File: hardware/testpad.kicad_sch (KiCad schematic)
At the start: 14 parts, among them U2 ESP32-C6-WROOM-1, U3 TPS62840YBGR

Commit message: :construction: sync components
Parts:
- removed D1: LED, symbol components:XL-6028RGBW-WS2812B
- removed L1: 22uH,5mA, PCM_JLCPCB:L_0805, symbol components:22uH,5mA
- removed R2: 10kΩ, KeysDock:R_0402, symbol components:0402,10kΩ
- added L1: 22uH,5mA, KeysDock:IND-SMD_L2.5-W2.0_MHCHL2520, symbol components:FTC252012S2R2MBCA
- added R3: 267kΩ, KeysDock:R_0402, symbol components:0402,267kΩ
- U3: footprint TPS62840YBGR:BGA6N40P3X2_146X96X50N -> KeysDock:BGA6N40P3X2_146X96X50N
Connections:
- net +3.3V: now also R1.2, U3.A2 (VOS), L1.2; no longer R1.1
- net +5V: now also U3.C1 (EN)
- net GND: now also U3.A1 (GND), R3.1
- net at SW1.H1 (HE_V3.3): now also R1.1; no longer R1.2
- net at U3.B2 (SW): now also L1.1
- net at U3.C2 (VSET): now also R3.2
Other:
- moved on the sheet: C1, C2, C3, U3

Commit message: :construction: typeboard routing
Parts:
- removed R1: 10kΩ, KeysDock:R_0402, symbol components:0402,10kΩ
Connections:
- net +3.3V: now also SW1.H1 (HE_V3.3)
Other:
- moved on the sheet: SW1, SW2, SW3, SW4

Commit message: :construction: try controller
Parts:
- SW1, SW2, SW3, SW4: footprint KeysDock:KD-SINGLE-KEY -> KeysDock:KD-SINGLE-KEY_LED; symbol components:KD_SINGLE_KEY -> components:KD_SINGLE_KEY_LED
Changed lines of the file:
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@@
 	)
 	(symbol
-		(lib_id "components:KD_SINGLE_KEY")
+		(lib_id "components:KD_SINGLE_KEY_LED")
 		(at 85.09 45.72 0)
 		(unit 1)
@@
 			)
 		)
-		(property "Footprint" "KeysDock:KD-SINGLE-KEY"
+		(property "Footprint" "KeysDock:KD-SINGLE-KEY_LED"
 			(at 85.09 34.29 0)
 			(show_name yes)
@@
 	)
 	(symbol
-		(lib_id "components:KD_SINGLE_KEY")
+		(lib_id "components:KD_SINGLE_KEY_LED")
 		(at 128.27 45.72 0)
 		(unit 1)
@@
 			)
 		)
-		(property "Footprint" "KeysDock:KD-SINGLE-KEY"
+		(property "Footprint" "KeysDock:KD-SINGLE-KEY_LED"
 			(at 128.27 34.29 0)
 			(show_name yes)
@@
 	)
 	(symbol
-		(lib_id "components:KD_SINGLE_KEY")
+		(lib_id "components:KD_SINGLE_KEY_LED")
 		(at 171.45 45.72 0)
 		(unit 1)
@@
 			)
 		)
-		(property "Footprint" "KeysDock:KD-SINGLE-KEY"
+		(property "Footprint" "KeysDock:KD-SINGLE-KEY_LED"
 			(at 171.45 34.29 0)
 			(show_name yes)
@@
 	)
 	(symbol
-		(lib_id "components:KD_SINGLE_KEY")
+		(lib_id "components:KD_SINGLE_KEY_LED")
 		(at 213.36 45.72 0)
 		(unit 1)
@@
 			)
 		)
-		(property "Footprint" "KeysDock:KD-SINGLE-KEY"
+		(property "Footprint" "KeysDock:KD-SINGLE-KEY_LED"
 			(at 213.36 34.29 0)
 			(show_name yes)

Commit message: :sparkles: add sheet template
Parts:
- removed C1: 4.7uF, KeysDock:C_0402, symbol components:0402,4.7uF
- removed C2: 10uF, KeysDock:C_0402, symbol components:0402,10uF
- removed C3: 22uF, KeysDock:C_0603, symbol components:0603,22uF
- removed L1: 22uH,5mA, KeysDock:IND-SMD_L2.5-W2.0_MHCHL2520, symbol components:FTC252012S2R2MBCA
- removed R3: 267kΩ, KeysDock:R_0402, symbol components:0402,267kΩ
- removed S1: Tactile Button, 160gf, KeysDock:SW_TS-1088-AR02016, symbol components:Tactile Button, 160gf, 12V, 50mA, 4.0mm
- removed SW1, SW2, SW3, SW4: ~, KeysDock:KD-SINGLE-KEY_LED, symbol components:KD_SINGLE_KEY_LED
- removed U2: ESP32-C6-WROOM-1, PCM_Espressif:ESP32-C6-WROOM-1, symbol components:ESP32-C6-WROOM-1
- removed U3: TPS62840YBGR, KeysDock:BGA6N40P3X2_146X96X50N, symbol components:TPS62840YBGR
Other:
- note removed: "RESET MCU"

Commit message: :sparkles: add testboard
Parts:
- added C1, C14: 4.7uF, KeysDock:C_0402, symbol components:0402,4.7uF
- added C10: 22uF, KeysDock:C_0402, symbol components:0402,22uF
- added C11, C15, C2, C3: 1uF, KeysDock:C_0402, symbol components:0402,1uF
- added C4, C5, C6, C7: 100nF, KeysDock:C_0402, symbol components:0402,100nF
- added C8: 10uF, KeysDock:C_0402, symbol components:0402,10uF
- added C9: 3.3nF, KeysDock:C_0402, symbol components:0402,3.3nF
- added D1: SM4007PL, KeysDock:D_SOD-123FL, symbol components:SM4007PL
- added J1: Connector, USB-TYPE-C-16P, KeysDock:HC-TYPE-C-16P-CB1.6, symbol components:HC-TYPE-C-16P-CB1.6
- added J3: AFA01-S08FCA-00, KeysDock:AFA01-S08FCA-00, symbol components:AFA01-S08FCA-00
- added L1: 2.2uH,5mA, KeysDock:IND-SMD_L2.5-W2.0_MHCHL2520, symbol components:FTC252012S2R2MBCA
- added LED1: ~, KeysDock:XL-3512RGBW-WS2812B, symbol components:XL-3512RGBW-WS2812B
- added LED2, LED3, LED4, LED5: ~, KeysDock:XL-6028RGBW-WS2812B, symbol components:XL-6028RGBW-WS2812B
- added PC1: ~, KeysDock:HC-1.25-4PWT, symbol components:HC-1.25-4PWT
- added PC2: ~, KeysDock:HC-1.25-2PWT, symbol components:HC-1.25-2PWT
- added R1, R12, R9: 10kΩ, KeysDock:R_0402, symbol components:0402,10kΩ
- added R10: 0Ω, KeysDock:R_0402, symbol components:0402,0Ω
- added R11: 3kΩ, KeysDock:R_0402, symbol components:0402,3kΩ
- added R13, R14, R5, R6: 100Ω, KeysDock:R_0402, symbol components:0402,100Ω
- added R2, R4: 4.7kΩ, KeysDock:R_0402, symbol components:0402,4.7kΩ
- added R3: 100kΩ, KeysDock:R_0402, symbol components:0402,100kΩ
- added R7: 1.78kΩ, KeysDock:R_0402, symbol components:0402,1.78kΩ
- added R8: 1.54kΩ, KeysDock:R_0402, symbol components:0402,1.54kΩ
- added S1: Reset, 160gf, KeysDock:TS24CA, symbol components:TS24CA
- added S2: ~, KeysDock:EC12E1240301, symbol components:EC12E1240301
- added S3: Joint Download, 160gf, KeysDock:SW_TS-1088-AR02016, symbol components:Tactile Button, 160gf, 12V, 50mA, 4.0mm
- added SW1: ~, KeysDock:SW-SMD_SSSS811101, symbol components:SSSS811101
- added SW2, SW3, SW4, SW5: ~, KeysDock:KD-SINGLE-KEY, symbol components:KD_SINGLE_KEY
- added T1: ~, KeysDock:XL4067TS, symbol components:XL4067TS
- added U1: ESP32-C6-WROOM-1, KeysDock:ESP32-C6-WROOM-1, symbol components:ESP32-C6-WROOM-1
- added U2: BQ24074RGTR, KeysDock:QFN50P300X300X80-17N, symbol components:BQ24074RGTR
- added U3: TLA2518IRTER, KeysDock:QFN50P300X300X80-17N, symbol components:TLA2518IRTER
- added U6: TPS62142RGTR, KeysDock:QFN50P300X300X80-17N, symbol components:TPS62142RGTR
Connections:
- new net: R6.1, S3.1 (A)
- new net: LED3.L4 (DO), LED4.L2 (DI)
- new net: LED4.L4 (DO), LED5.L2 (DI)
- new net: R7.2, U2.16 (ISET)
- new net: C3.1, U3.8 (DECAP)
- new net: D1.1 (K), PC2.2, SW1.1 (OUT1)
- new net: D1.2 (A), SW1.3 (OUT2)
- new net: R1.2, U2.1 (TS)
- new net: R8.2, U2.12 (ILIM)
- new net: R11.1, U2.15 (ITERM)
- new net: J1.A5 (CC1), R4.1
- new net: J1.B5 (CC2), R2.1
- new net: C9.1, U6.9 (SS/TR)
- new net: LED5.L4 (DO), R14.1
- new net: LED2.L4 (DO), LED3.L2 (DI)
- new net: R3.2, U6.4 (PG)
- new net: SW4.H3 (HE_VOUT), T1.8 (Y1)
- new net: LED1.L4 (DI), R13.2
- new net: R5.1, S1.1 (A)
- new net: SW3.H3 (HE_VOUT), T1.7 (Y2)
- new net: SW2.H3 (HE_VOUT), T1.6 (Y3)
- new net: SW5.H3 (HE_VOUT), T1.9 (Y0)
- new net: R13.1, U1.20 (GPIO22)
- new net: L1.1, U6.1 (SW_1), U6.2 (SW_2), U6.3 (SW_3)
- new net BAT_CHG: U1.5 (MTDI/GPIO5/ADC1_CH5), U2.9 (~{CHG})
- new net BOOT_0: S3.2 (B), U1.15 (GPIO9)
- new net BOOT_1: U1.10 (GPIO8)
- new net EN: S1.2 (B), U1.3 (EN/CHIP_PU)
- new net KEYS_CH_A: T1.10 (A), U1.11 (GPIO10)
- new net KEYS_CH_B: T1.11 (B), U1.12 (GPIO11)
- new net KEYS_CH_C: T1.14 (C), U1.23 (GPIO15)
- new net KEYS_CH_CE: T1.15 (E#), U1.21 (GPIO23)
- new net KEYS_CH_D: T1.13 (D), U1.16 (GPIO18)
- new net KEYS_DT_1: T1.1 (Z), U3.1 (AIN2/GPIO2)
- new net P,+3.3: C10.1, C11.2, C2.1, C4.1, C5.1, C6.1, C7.1, J3.2, L1.2, R12.1, R3.1, R9.1, SW2.H1 (HE_V3.3), SW3.H1 (HE_V3.3), SW4.H1 (HE_V3.3), SW5.H1 (HE_V3.3), T1.16 (Y15), T1.17 (Y14), T1.18 (Y13), T1.19 (Y12), T1.2 (Y7), T1.20 (Y11), T1.21 (Y10), T1.22 (Y9), T1.23 (Y8), T1.24 (VCC), T1.3 (Y6), T1.4 (Y5), T1.5 (Y4), U1.2 (3V3), U3.10 (DVDD), U3.2 (AIN3/GPIO3), U3.3 (AIN4/GPIO4), U3.4 (AIN5/GPIO5), U3.5 (AIN6/GPIO6), U3.7 (AVDD), U6.14 (VOS)
- new net P,+5: C14.2, C8.1, LED1.L3 (VCC), LED2.L3 (VCC), LED3.L3 (VCC), LED4.L3 (VCC), LED5.L3 (VCC), U2.10 (OUT_10), U2.11 (OUT_11), U2.5 (EN2), U6.10 (AVIN), U6.11 (PVIN_11), U6.12 (PVIN_12), U6.13 (EN)
- new net P,E: C1.1, C10.2, C14.1, C15.2, C4.2, C5.2, C6.2, C7.2, C8.2, J1.A12B1 (GND), J1.B12A1 (GND), J1.S1 (SHIELD), J3.1, J3.MP1, J3.MP2, LED1.L1 (GND), LED2.L1 (GND), LED3.L1 (GND), LED4.L1 (GND), LED5.L1 (GND), PC1.4, PC2.1, R1.1, R10.2, R11.2, R14.2, R2.2, R4.2, R5.2, R6.2, R7.1, R8.1, S2.C, SW1.4 (GND), SW1.5 (GND), SW1.6 (GND), SW1.7 (GND), U1.1 (GND), U1.28 (GND), U1.29 (GND), U2.14 (TMR), U2.17 (EXP), U2.4 (~{CE}), U2.6 (EN1), U2.8 (VSS), U3.17 (GND), U6.15 (PGND_15), U6.16 (PGND_16), U6.17 (EXP), U6.5 (FB), U6.7 (FSW), U6.8 (DEF)
- new net P,GND: C11.1, C2.2, C3.2, C9.2, R10.1, SW2.H2 (GND), SW2.H5 (GND), SW3.H2 (GND), SW3.H5 (GND), SW4.H2 (GND), SW4.H5 (GND), SW5.H2 (GND), SW5.H5 (GND), T1.12 (GND), U3.15 (AIN0/GPIO0), U3.16 (AIN1/GPIO1), U3.9 (GND), U6.6 (AGND)
- new net RANA: SW2.H4 (HE_SLEEP), SW3.H4 (HE_SLEEP), SW4.H4 (HE_SLEEP), SW5.H4 (HE_SLEEP), U1.19 (GPIO21)
- new net SAKI_MOVE: SW2.H6 (HE_AWAKE), SW3.H6 (HE_AWAKE), SW4.H6 (HE_AWAKE), SW5.H6 (HE_AWAKE), U1.26 (GPIO3/ADC1_CH3)
- new net SPI_CLK: J3.3, U1.6 (MTCK/GPIO6/ADC1_CH6), U3.13 (SCLK)
- new net SPI_CS3_ADC: U1.17 (GPIO19), U3.11 (*CS)
- new net SPI_CS4_EINK: J3.7, U1.18 (GPIO20)
- new net SPI_MISO: U1.27 (GPIO2/ADC1_CH2), U3.12 (SDO)
- new net SPI_MOSI: J3.4, U1.7 (MTDO/GPIO7), U3.14 (SDI)
- new net TOMO0: LED1.L2 (DO), LED2.L2 (DI)
- new net U0RX: PC1.2, U1.24 (U0RXD/GPIO17)
- new net U0TX: PC1.3, U1.25 (U0TXD/GPIO16)
- new net USB_D+: J1.A6 (D+), J1.B6 (D+), U1.14 (GPIO13/USB_D+)
- new net USB_D-: J1.A7 (D-), J1.B7 (D-), U1.13 (GPIO12/USB_D-)
- new net USB_PWR_SUPP: C15.1, J1.A9B4 (VBUS), J1.B9A4 (VBUS), PC1.1, U2.13 (IN)
- new net VBAT: C1.2, SW1.2 (IN), U2.2 (BAT_2), U2.3 (BAT_3), U3.6 (AIN7/GPIO7)
- new net WHEEL_A: R9.2, S2.A, U1.8 (GPIO0/ADC1_CH0/XTAL_32K_P)
- new net WHEEL_B: R12.2, S2.B, U1.9 (GPIO1/ADC1_CH1/XTAL_32K_N)
- no-connect marks 0 -> 5
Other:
- note added: "GNDA"
- note added: "GNDD"
- note added: "GND_BAT"

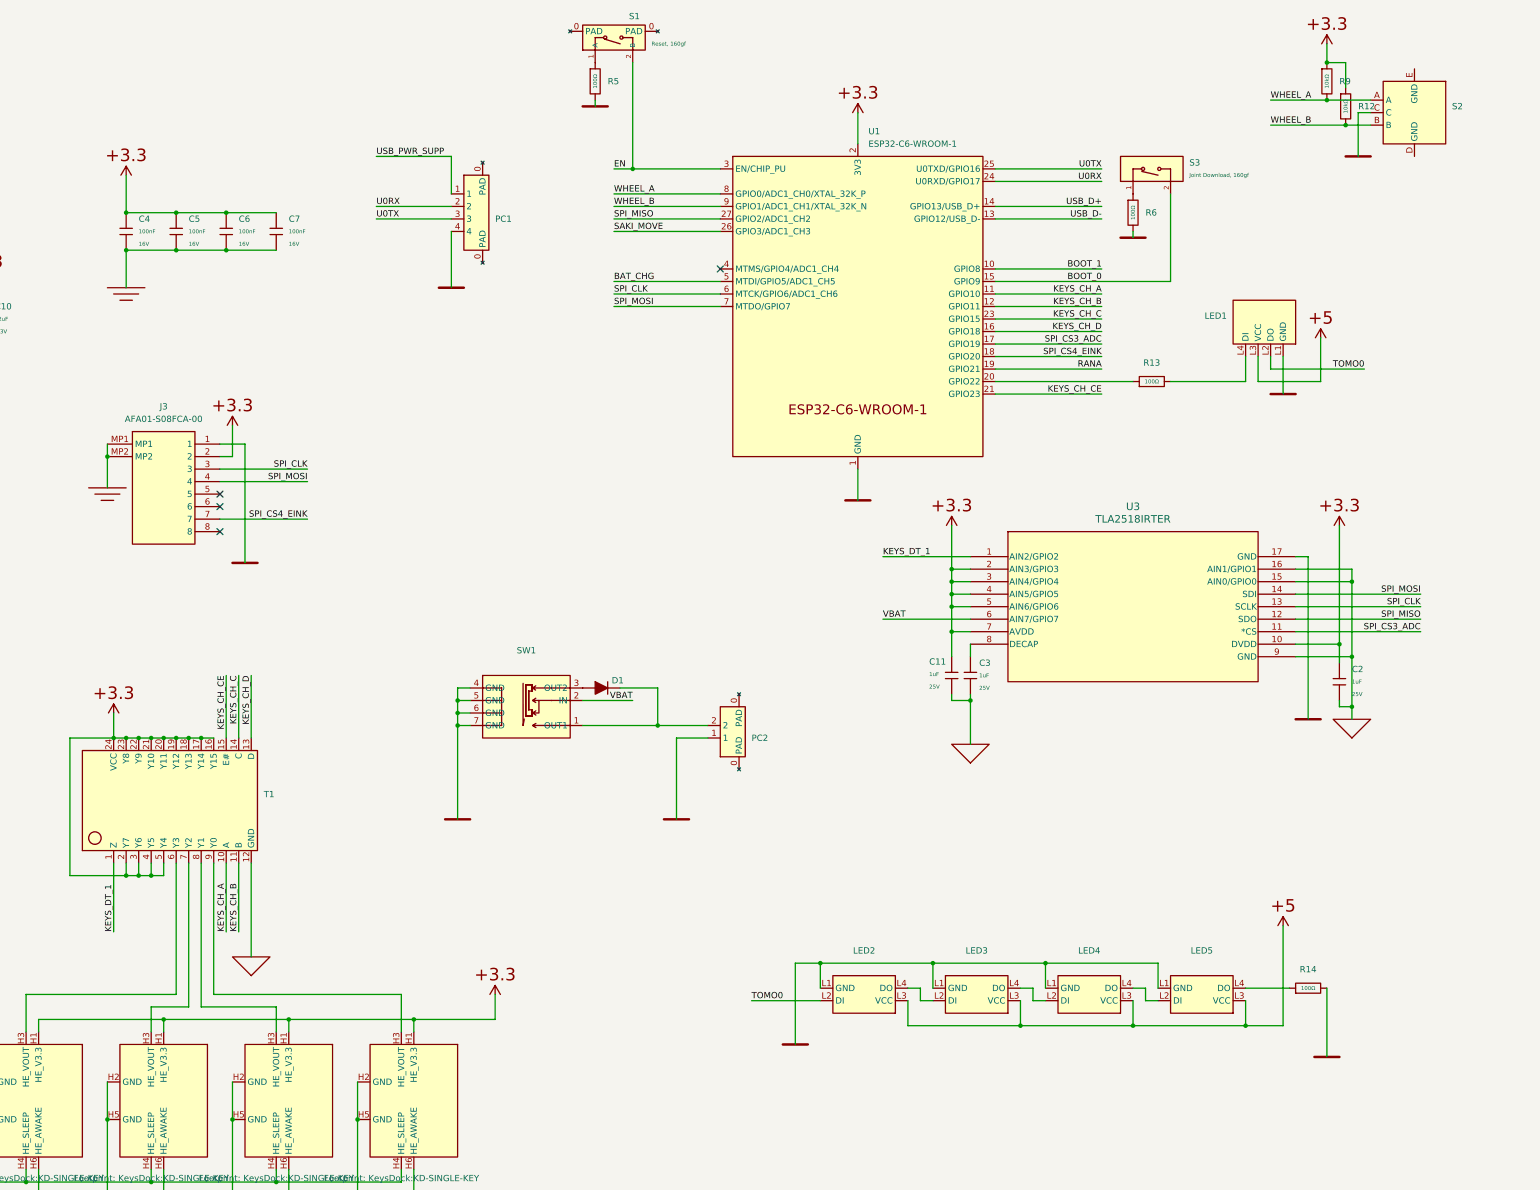
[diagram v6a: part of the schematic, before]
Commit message: :sparkles: add bom table
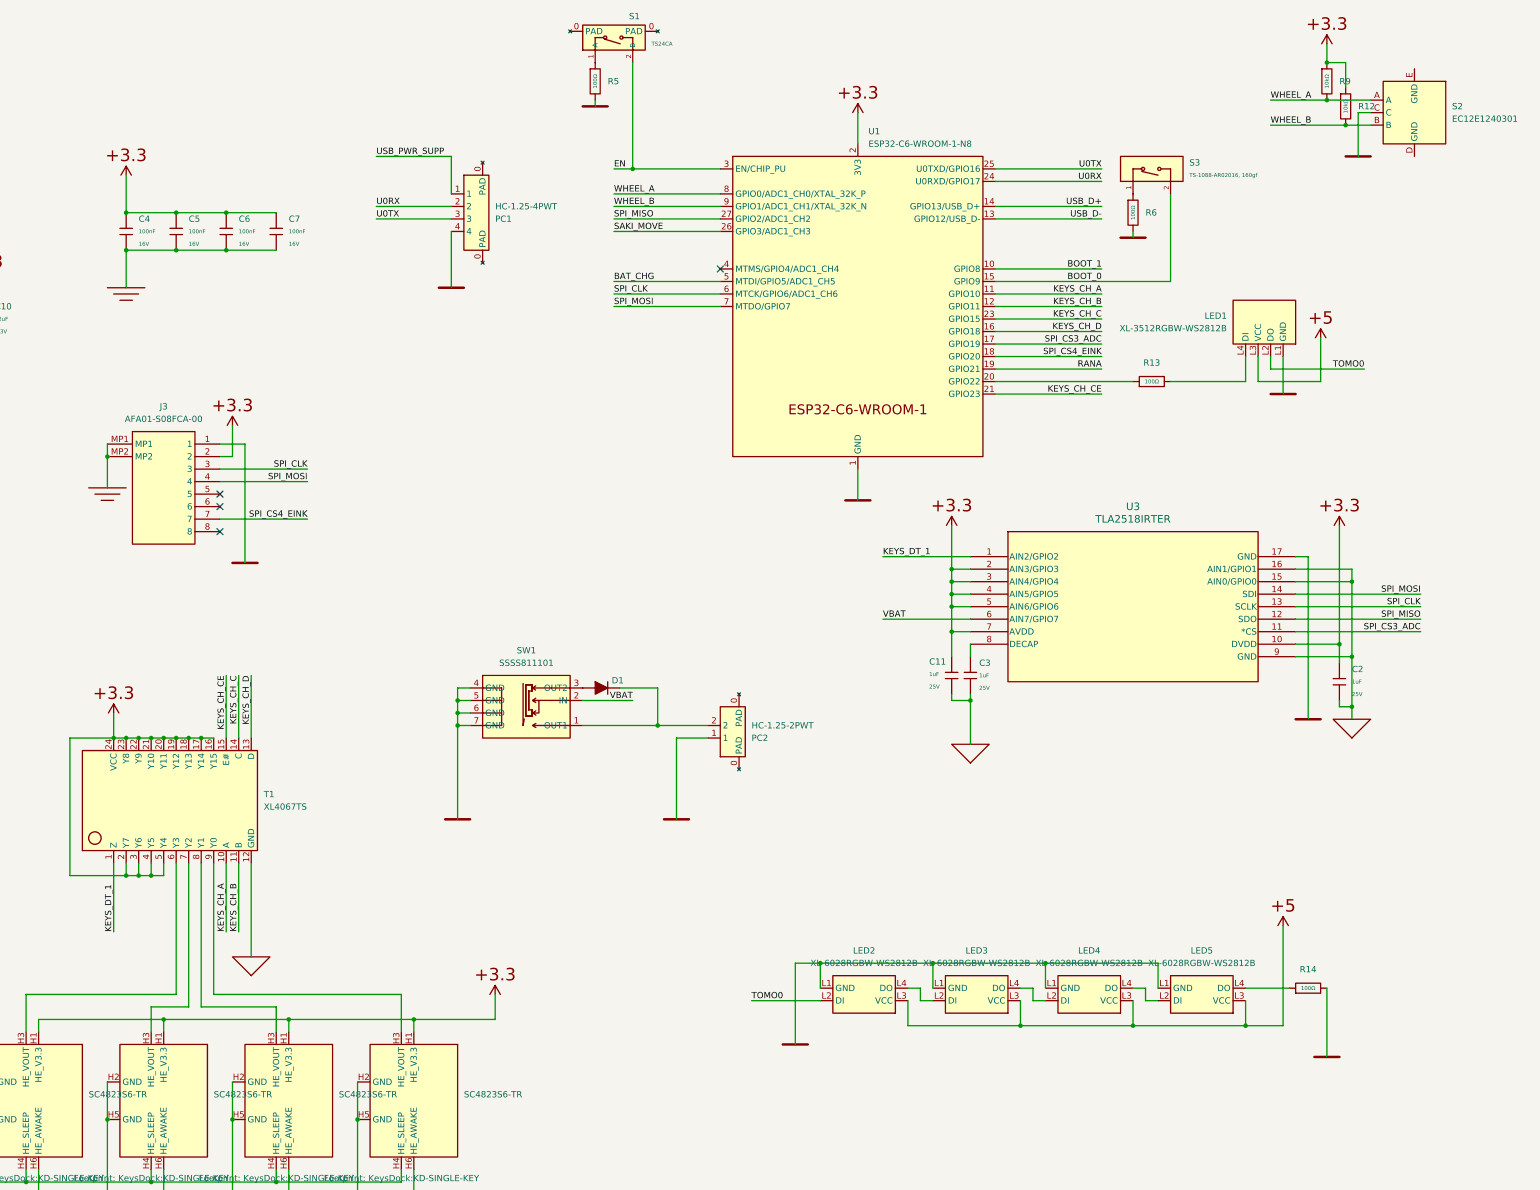
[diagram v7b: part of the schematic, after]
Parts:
- D1: LCSC (none) -> C78741; Manufacturer (none) -> MCC(美微科)
- J1: value Connector, USB-TYPE-C-16P -> HC-TYPE-C-16P-CB1.6; LCSC C2927039 -> C2894902; Manufacturer (none) -> HCTL(华灿天禄)
- J3: LCSC (none) -> C262755; Manufacturer (none) -> JUSHUO; PartNumber (none) -> AFA01-S08FCA-00
- LED1: value ~ -> XL-3512RGBW-WS2812B; LCSC (none) -> C49237874; Manufacturer (none) -> XINGLIGHT(成兴光)
- LED2, LED3, LED4, LED5: value ~ -> XL-6028RGBW-WS2812B; LCSC (none) -> C42163197; Manufacturer (none) -> XINGLIGHT(成兴光)
- PC1: value ~ -> HC-1.25-4PWT; LCSC (none) -> C2845381; Manufacturer (none) -> HCTL(华灿天禄)
- PC2: value ~ -> HC-1.25-2PWT; LCSC (none) -> C2845379; Manufacturer (none) -> HCTL(华灿天禄)
- S1: value Reset, 160gf -> TS24CA; LCSC C720477 -> C393942; Manufacturer XUNPU -> SHOU HAN(首韩)
- S2: value ~ -> EC12E1240301; LCSC (none) -> C351235; Manufacturer (none) -> ALPSALPINE
- S3: value Joint Download, 160gf -> TS-1088-AR02016, 160gf
- SW1: value ~ -> SSSS811101; LCSC (none) -> C109335; Manufacturer (none) -> ALPSALPINE
- SW2, SW3, SW4, SW5: value ~ -> SC4823S6-TR; LCSC (none) -> C52021064; Manufacturer (none) -> Semiment(赛卓)
- T1: value ~ -> XL4067TS; LCSC (none) -> C41427445; Manufacturer (none) -> XINLUDA
- U1: value ESP32-C6-WROOM-1 -> ESP32-C6-WROOM-1-N8; Manufacturer (none) -> Espressif Systems
- U2: Height (none) -> 1mm; LCSC (none) -> C54313; Manufacturer (none) -> Texas Instruments; Standard (none) -> IPC 7351B
- U3: LCSC (none) -> C1855741; Manufacturer (none) -> Texas Instruments
- U6: LCSC (none) -> C129331; Manufacturer (none) -> Texas Instruments
